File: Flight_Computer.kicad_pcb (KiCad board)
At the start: 4 copper layers, 75.8 x 76.2 mm, 142 parts, among them IC1 PIC32MZ2048EFH144-I_PL, IC2 FAN4010IL6X_F113, IC3 FAN4010IL6X_F113, J1 ICSP Programming, J2 SC_19-20, J3 UJ2-MBH-1-SMT-TR, J4 47219-2001, Q1 Q_NPN_BEC, Q2 Q_NPN_BEC, U1 STMPS2141STR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

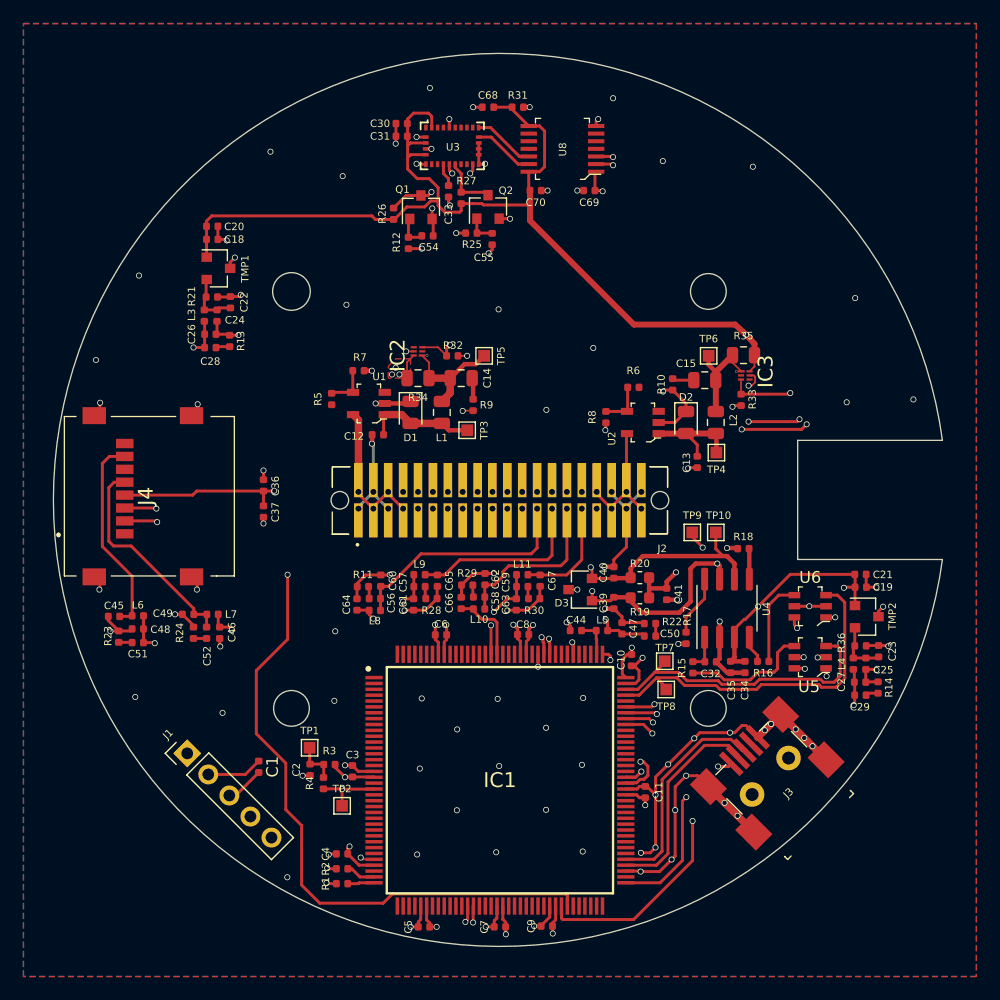
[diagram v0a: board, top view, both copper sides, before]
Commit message: Major changes to routing and fixed filters
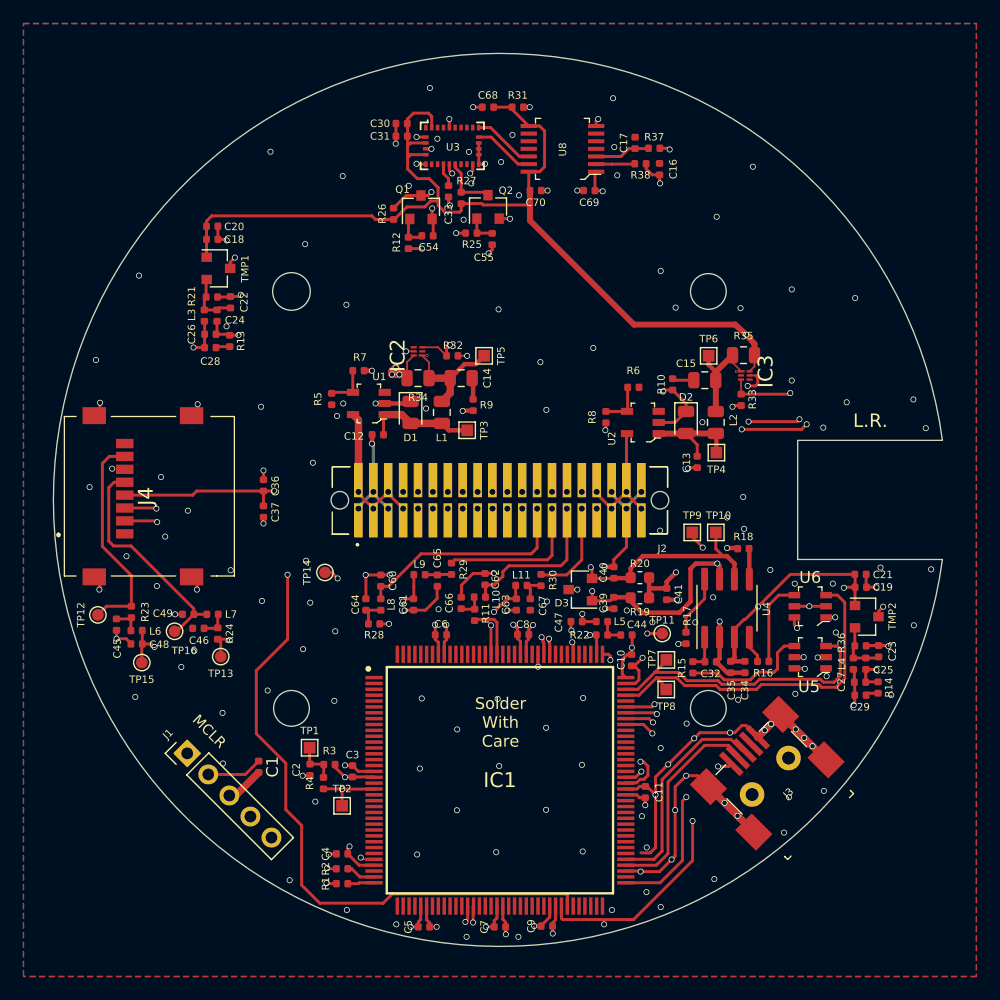
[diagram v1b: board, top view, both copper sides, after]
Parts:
- removed C50, C51, C52, C56, C57, C58, C59: 1u, Capacitor_SMD:C_0402_1005Metric
- added C16: 1n, Capacitor_SMD:C_0402_1005Metric, F.Cu at (166.0, 98.8)
- added C17: 1n, Capacitor_SMD:C_0402_1005Metric, F.Cu at (163.9, 96.5)
- added R37: 470, Resistor_SMD:R_0402_1005Metric, F.Cu at (165.6, 97.0)
- added R38: 470, Resistor_SMD:R_0402_1005Metric, F.Cu at (164.4, 98.3)
- added TP11: T, TestPoint:TestPoint_Pad_D1.0mm, F.Cu at (166.2, 138.4)
- added TP12: T, TestPoint:TestPoint_Pad_D1.0mm, F.Cu at (118.1, 136.8)
- added TP13: T, TestPoint:TestPoint_Pad_D1.0mm, F.Cu at (128.6, 140.4)
- added TP14: T, TestPoint:TestPoint_Pad_D1.0mm, F.Cu at (137.5, 133.2)
- added TP15: T, TestPoint:TestPoint_Pad_D1.0mm, F.Cu at (121.9, 140.9)
- added TP16: T, TestPoint:TestPoint_Pad_D1.0mm, F.Cu at (124.7, 138.2)
- C44, C45, C46: value 1n -> 330p
- C47, C48, C49, C60, C61, C62, C63: value 10n -> NP
- L10, L11, L5, L6, L7, L8, L9: value 220n -> 0
- R11, R22, R23, R24, R28, R29, R30: value 3.3 -> 470
- R21, R36: value 3.3k -> NP
- moved R11 9.83 mm to (150.2, 136.8), turned to 90 degrees
- moved R28 5.34 mm to (141.7, 137.6), turned to 180 degrees
- moved C44 4.33 mm to (163.2, 138.5), turned to 180 degrees
- moved R22 4.22 mm to (161.1, 138.5), turned to 0 degrees
- moved C47 3.92 mm to (158.9, 137.4), turned to 0 degrees
- moved R23 2.37 mm to (121.0, 136.6), turned to 270 degrees
- moved C67 2.20 mm to (155.0, 135.9)
- moved R24 2.07 mm to (128.3, 138.4)
- moved R29 1.93 mm to (148.3, 132.9), turned to 90 degrees
- moved C46 1.86 mm to (126.7, 138.0), turned to 0 degrees
- moved R30 1.68 mm to (155.9, 133.8), turned to 90 degrees
- moved C48 1.29 mm to (121.4, 139.3)
- moved L6 1.26 mm to (121.4, 138.1)
- moved L10 1.02 mm to (150.7, 135.3)
- moved L11 0.92 mm to (154.2, 134.3)
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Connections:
- C44 pad 2: SDO -> Net-(C44-Pad2)
- C45 pad 2: SD_MISO -> Net-(C45-Pad2)
- C46 pad 2: SCK -> Net-(C46-Pad2)
- C64 pad 2: UART1_TX -> Net-(C64-Pad2)
- C66 pad 2: UART2_TX -> Net-(C66-Pad2)
- J2 pad 27: Net-(C65-Pad2) -> Net-(J2-Pad27)
- J2 pad 31: Net-(C67-Pad2) -> Net-(J2-Pad31)
- L10 pad 1: UART2_TX -> Net-(C66-Pad2)
- L5 pad 1: SDO -> Net-(C44-Pad2)
- L6 pad 1: SD_MISO -> Net-(C45-Pad2)
- L7 pad 1: SCK -> Net-(C46-Pad2)
- L8 pad 1: UART1_TX -> Net-(C64-Pad2)
- R11 pad 1: Net-(C56-Pad1) -> UART2_TX
- R11 pad 2: GND -> Net-(C66-Pad2)
- R22 pad 1: Net-(C50-Pad1) -> SDO
- R22 pad 2: GND -> Net-(C44-Pad2)
- R23 pad 1: Net-(C51-Pad1) -> SD_MISO
- R23 pad 2: GND -> Net-(C45-Pad2)
- R24 pad 1: Net-(C52-Pad1) -> SCK
- R24 pad 2: GND -> Net-(C46-Pad2)
- R28 pad 1: Net-(C57-Pad1) -> UART1_TX
- R28 pad 2: GND -> Net-(C64-Pad2)
- R29 pad 1: Net-(C58-Pad1) -> Net-(C65-Pad2)
- R29 pad 2: GND -> Net-(J2-Pad27)
- R30 pad 1: Net-(C59-Pad1) -> Net-(C67-Pad2)
- R30 pad 2: GND -> Net-(J2-Pad31)
- U8 pad 2: BNO_TX -> Net-(R38-Pad1)
- U8 pad 3: BNO_RX -> Net-(C17-Pad2)
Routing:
- net Net-(C65-Pad2): track 15.5 -> 2.27 mm
- net Net-(J2-Pad27): track 0.00 -> 12.8 mm
- net GND: track 185.9 -> 176.7 mm, vias 115 -> 189
- net Net-(J2-Pad31): track 0.00 -> 8.40 mm
- net BNO_RX: track 77.7 -> 70.2 mm
- net Net-(C67-Pad2): track 9.51 -> 2.46 mm
- net BNO_TX: track 77.1 -> 71.1 mm
- net SDO: track 3.29 -> 8.40 mm, vias 0 -> 2
- net Net-(C17-Pad2): track 0.00 -> 4.75 mm
- net Net-(R38-Pad1): track 0.00 -> 3.31 mm
- net SD_MOSI: track 50.0 -> 47.1 mm, vias 2 -> 3
- net +3V3: track 52.5 -> 55.3 mm
- net UART1_TX: track 18.4 -> 15.8 mm
- net Net-(C64-Pad2): track 0.00 -> 2.52 mm
- net Net-(C45-Pad2): track 0.00 -> 2.43 mm
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- removed copper zone on F.Cu, net +3V3
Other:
- board text added: "L.R."
- board text added: "MASA-Dearborn 2020"
- board text added: "MCLR"
- board text added: "Solder With Care"

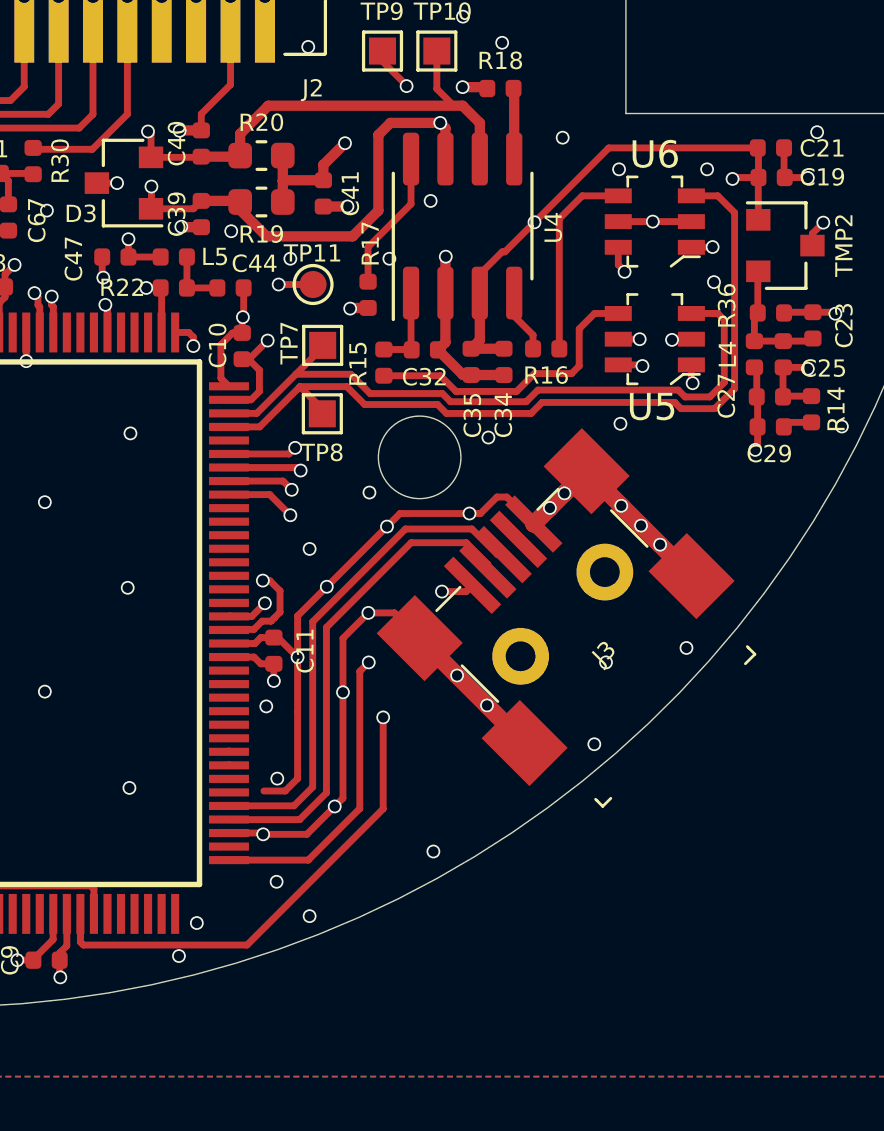
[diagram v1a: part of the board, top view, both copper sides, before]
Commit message: Adjusted a few vias to satisfy DRC
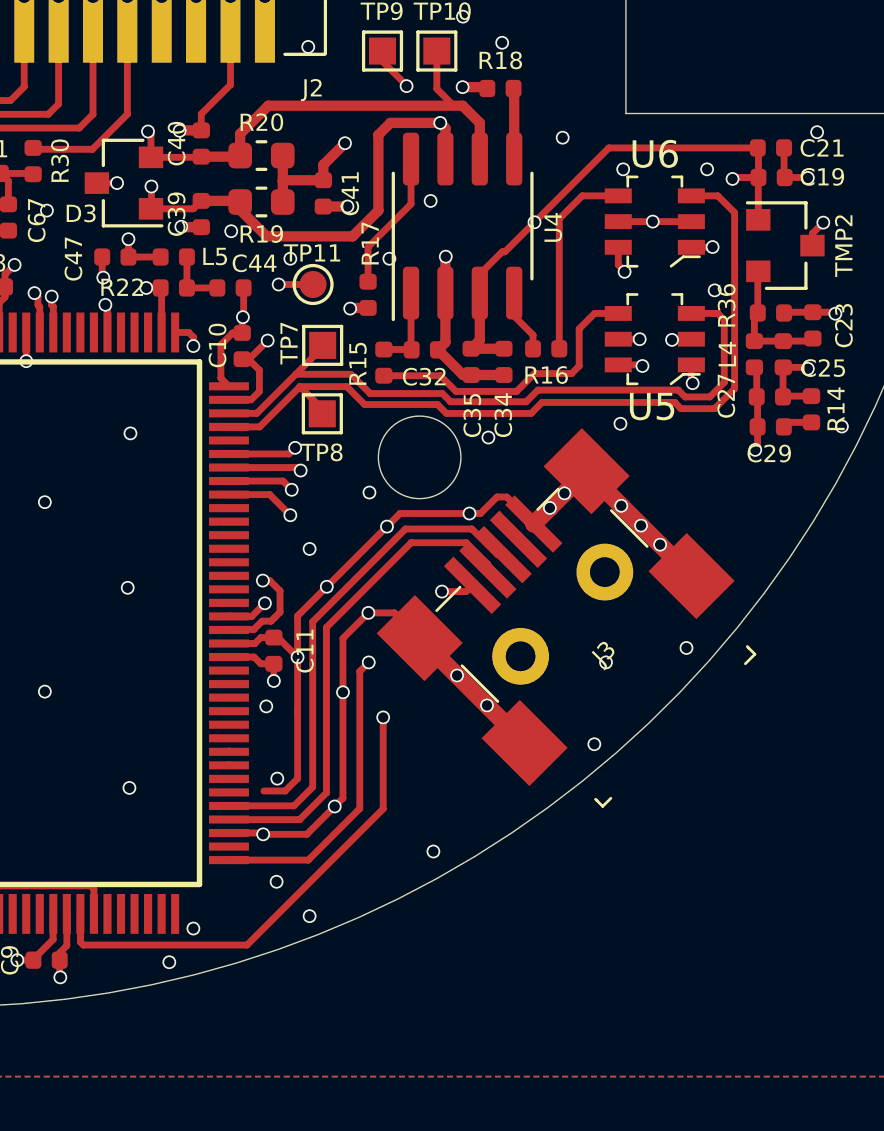
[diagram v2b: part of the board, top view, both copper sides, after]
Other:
- rule trace_min: 0.1016 -> 0.127
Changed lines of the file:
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@@
   )
   (setup
-    (last_trace_width 0.254)
+    (last_trace_width 0.1524)
     (user_trace_width 0.254)
     (user_trace_width 0.381)
@@
     (zone_clearance 0.1524)
     (zone_45_only no)
-    (trace_min 0.1016)
+    (trace_min 0.127)
     (via_size 0.508)
     (via_drill 0.381)
@@
   (via (at 170.688 159.338) (size 0.508) (drill 0.381) (layers F.Cu B.Cu) (net 1))
   (via (at 164.8968 160.4556) (size 0.508) (drill 0.381) (layers F.Cu B.Cu) (net 1))
-  (via (at 161.9504 161.9796) (size 0.508) (drill 0.381) (layers F.Cu B.Cu) (net 1))
+  (via (at 161.8234 162.1828) (size 0.508) (drill 0.381) (layers F.Cu B.Cu) (net 1))
   (via (at 153.9748 164.2656) (size 0.508) (drill 0.381) (layers F.Cu B.Cu) (net 1))
   (via (at 149.5552 164.2656) (size 0.508) (drill 0.381) (layers F.Cu B.Cu) (net 1))
@@
   (via (at 152.5016 98.1748) (size 0.508) (drill 0.381) (layers F.Cu B.Cu) (net 1))
   (via (at 180.7972 134.1412) (size 0.508) (drill 0.381) (layers F.Cu B.Cu) (net 1))
-  (via (at 177.546 134.1412) (size 0.508) (drill 0.381) (layers F.Cu B.Cu) (net 1))
-  (via (at 181.0512 138.3068) (size 0.508) (drill 0.381) (layers F.Cu B.Cu) (net 1))
+  (via (at 177.6984 134.1412) (size 0.508) (drill 0.381) (layers F.Cu B.Cu) (net 1))
+  (via (at 181.0766 138.6116) (size 0.508) (drill 0.381) (layers F.Cu B.Cu) (net 1))
   (via (at 147.066 96.1936) (size 0.508) (drill 0.381) (layers F.Cu B.Cu) (net 1))
   (via (at 149.7584 97.3112) (size 0.508) (drill 0.381) (layers F.Cu B.Cu) (net 1))
@@
   (segment (start 129.861898 152.211302) (end 131.826 150.2472) (width 0.635) (layer F.Cu) (net 1))
   (segment (start 129.322102 152.211302) (end 129.861898 152.211302) (width 0.635) (layer F.Cu) (net 1))
-  (via (at 161.29 163.1988) (size 0.508) (drill 0.381) (layers F.Cu B.Cu) (net 1))
+  (via (at 160.9344 163.4274) (size 0.508) (drill 0.381) (layers F.Cu B.Cu) (net 1))
   (via (at 139.3444 161.9796) (size 0.508) (drill 0.381) (layers F.Cu B.Cu) (net 1))
   (via (at 143.5608 163.1988) (size 0.508) (drill 0.381) (layers F.Cu B.Cu) (net 1))
@@
   (segment (start 175.4632 132.9728) (end 175.4632 109.046) (width 0.254) (layer In2.Cu) (net 124))
   (via (at 175.4632 132.9728) (size 0.508) (drill 0.381) (layers F.Cu B.Cu) (net 124))
-  (segment (start 160.609 98.3572) (end 161.955 98.3572) (width 0.254) (layer F.Cu) (net 223))
   (segment (start 172.5168 102.8738) (end 177.9778 108.3348) (width 0.254) (layer In2.Cu) (net 127))
   (segment (start 177.9778 108.3348) (end 177.9778 120.095) (width 0.254) (layer In2.Cu) (net 127))
@@
   (segment (start 155.8774 134.2936) (end 155.9052 134.3214) (width 0.254) (layer F.Cu) (net 191))
   (segment (start 154.7138 134.2936) (end 155.8774 134.2936) (width 0.254) (layer F.Cu) (net 191))
-  (segment (start 159.385 132.1092) (end 159.385 127.7442) (width 0.254) (layer F.Cu) (net 220))
-  (segment (start 158.092 133.4022) (end 159.385 132.1092) (width 0.254) (layer F.Cu) (net 220))
   (segment (start 147.12 113.9792) (end 147.851 114.7102) (width 0.1524) (layer F.Cu) (net 192))
   (segment (start 145.78 113.9792) (end 147.12 113.9792) (width 0.1524) (layer F.Cu) (net 192))
@@
   (segment (start 167.2614 116.7892) (end 167.132 116.6598) (width 0.254) (layer F.Cu) (net 209))
   (segment (start 168.9377 116.7892) (end 167.2614 116.7892) (width 0.254) (layer F.Cu) (net 209))
-  (segment (start 142.217 134.3952) (end 142.24 134.3722) (width 0.254) (layer F.Cu) (net 216))
-  (segment (start 155.067 131.6012) (end 155.575 131.0932) (width 0.254) (layer F.Cu) (net 216))
-  (segment (start 145.669 131.6012) (end 155.067 131.6012) (width 0.254) (layer F.Cu) (net 216))
-  (segment (start 155.575 131.0932) (end 155.575 127.7442) (width 0.254) (layer F.Cu) (net 216))
-  (segment (start 142.24 134.3722) (end 142.898 134.3722) (width 0.254) (layer F.Cu) (net 216))
-  (segment (start 142.898 134.3722) (end 145.669 131.6012) (width 0.254) (layer F.Cu) (net 216))
-  (segment (start 151.107 134.2682) (end 151.13 134.2452) (width 0.254) (layer F.Cu) (net 217))
-  (segment (start 151.13 134.2452) (end 151.915 134.2452) (width 0.254) (layer F.Cu) (net 217))
-  (segment (start 151.915 134.2452) (end 152.654 133.5062) (width 0.254) (layer F.Cu) (net 217))
-  (segment (start 152.654 133.5062) (end 152.654 133.1252) (width 0.254) (layer F.Cu) (net 217))
-  (segment (start 152.654 133.1252) (end 153.162 132.6172) (width 0.254) (layer F.Cu) (net 217))
-  (segment (start 153.162 132.6172) (end 157.607 132.6172) (width 0.254) (layer F.Cu) (net 217))
-  (segment (start 158.115 132.1092) (end 158.115 127.7442) (width 0.254) (layer F.Cu) (net 217))
-  (segment (start 157.607 132.6172) (end 158.115 132.1092) (width 0.254) (layer F.Cu) (net 217))
   (segment (start 176.6418 139.465) (end 177.5168 139.465) (width 0.254) (layer F.Cu) (net 211))
   (segment (start 175.7934 141.685) (end 176.0728 141.4056) (width 0.254) (layer F.Cu) (net 211))
@@
   (segment (start 128.3335 136.7979) (end 128.374 136.7574) (width 0.254) (layer F.Cu) (net 215))
   (segment (start 128.3335 137.9107) (end 128.3335 136.7979) (width 0.254) (layer F.Cu) (net 215))
+  (segment (start 142.217 134.3952) (end 142.24 134.3722) (width 0.254) (layer F.Cu) (net 216))
+  (segment (start 155.067 131.6012) (end 155.575 131.0932) (width 0.254) (layer F.Cu) (net 216))
+  (segment (start 145.669 131.6012) (end 155.067 131.6012) (width 0.254) (layer F.Cu) (net 216))
+  (segment (start 155.575 131.0932) (end 155.575 127.7442) (width 0.254) (layer F.Cu) (net 216))
+  (segment (start 142.24 134.3722) (end 142.898 134.3722) (width 0.254) (layer F.Cu) (net 216))
+  (segment (start 142.898 134.3722) (end 145.669 131.6012) (width 0.254) (layer F.Cu) (net 216))
   (segment (start 142.24 135.4342) (end 142.24 134.3722) (width 0.254) (layer F.Cu) (net 216))
+  (segment (start 151.107 134.2682) (end 151.13 134.2452) (width 0.254) (layer F.Cu) (net 217))
+  (segment (start 151.13 134.2452) (end 151.915 134.2452) (width 0.254) (layer F.Cu) (net 217))
+  (segment (start 151.915 134.2452) (end 152.654 133.5062) (width 0.254) (layer F.Cu) (net 217))
+  (segment (start 152.654 133.5062) (end 152.654 133.1252) (width 0.254) (layer F.Cu) (net 217))
+  (segment (start 152.654 133.1252) (end 153.162 132.6172) (width 0.254) (layer F.Cu) (net 217))
+  (segment (start 153.162 132.6172) (end 157.607 132.6172) (width 0.254) (layer F.Cu) (net 217))
+  (segment (start 158.115 132.1092) (end 158.115 127.7442) (width 0.254) (layer F.Cu) (net 217))
+  (segment (start 157.607 132.6172) (end 158.115 132.1092) (width 0.254) (layer F.Cu) (net 217))
   (segment (start 151.1705 134.2857) (end 151.13 134.2452) (width 0.254) (layer F.Cu) (net 217))
   (segment (start 151.1705 135.2842) (end 151.1705 134.2857) (width 0.254) (layer F.Cu) (net 217))
@@
   (segment (start 150.241 135.3247) (end 150.2005 135.2842) (width 0.254) (layer F.Cu) (net 219))
   (segment (start 150.241 136.3232) (end 150.241 135.3247) (width 0.254) (layer F.Cu) (net 219))
+  (segment (start 159.385 132.1092) (end 159.385 127.7442) (width 0.254) (layer F.Cu) (net 220))
+  (segment (start 158.092 133.4022) (end 159.385 132.1092) (width 0.254) (layer F.Cu) (net 220))
   (segment (start 155.956 133.4022) (end 155.9052 133.3514) (width 0.254) (layer F.Cu) (net 220))
   (segment (start 158.092 133.4022) (end 155.956 133.4022) (width 0.254) (layer F.Cu) (net 220))
@@
   (segment (start 165.0444 97.0342) (end 165.0722 97.0064) (width 0.254) (layer F.Cu) (net 222))
   (segment (start 163.9316 97.0342) (end 165.0444 97.0342) (width 0.254) (layer F.Cu) (net 222))
+  (segment (start 160.609 98.3572) (end 161.955 98.3572) (width 0.254) (layer F.Cu) (net 223))
   (segment (start 163.8738 98.3572) (end 161.955 98.3572) (width 0.254) (layer F.Cu) (net 223))
   (segment (start 163.9038 98.3272) (end 163.8738 98.3572) (width 0.254) (layer F.Cu) (net 223))
@@
     (connect_pads yes (clearance 0.1524))
     (min_thickness 0.1524)
-    (keepout (tracks not_allowed) (vias not_allowed) (copperpour not_allowed))
+    (keepout (tracks allowed) (vias not_allowed) (copperpour not_allowed))
     (fill (arc_segments 32) (thermal_gap 0.1524) (thermal_bridge_width 0.508))
     (polygon

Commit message: Fixed Vias
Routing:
- net GND: track 176.7 -> 175.4 mm, vias 189 -> 187
- net BNO_BL_IND: vias 3 -> 2
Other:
- net class Default: via_dia 0.508 -> 0.635; via_drill 0.381 -> 0.3048
- rule trace_min: 0.127 -> 0
- rule via_min_size: 0.3048 -> 0.635
